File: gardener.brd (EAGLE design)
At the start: 73.5 x 55 mm, 37 parts, among them IC2 REG1117

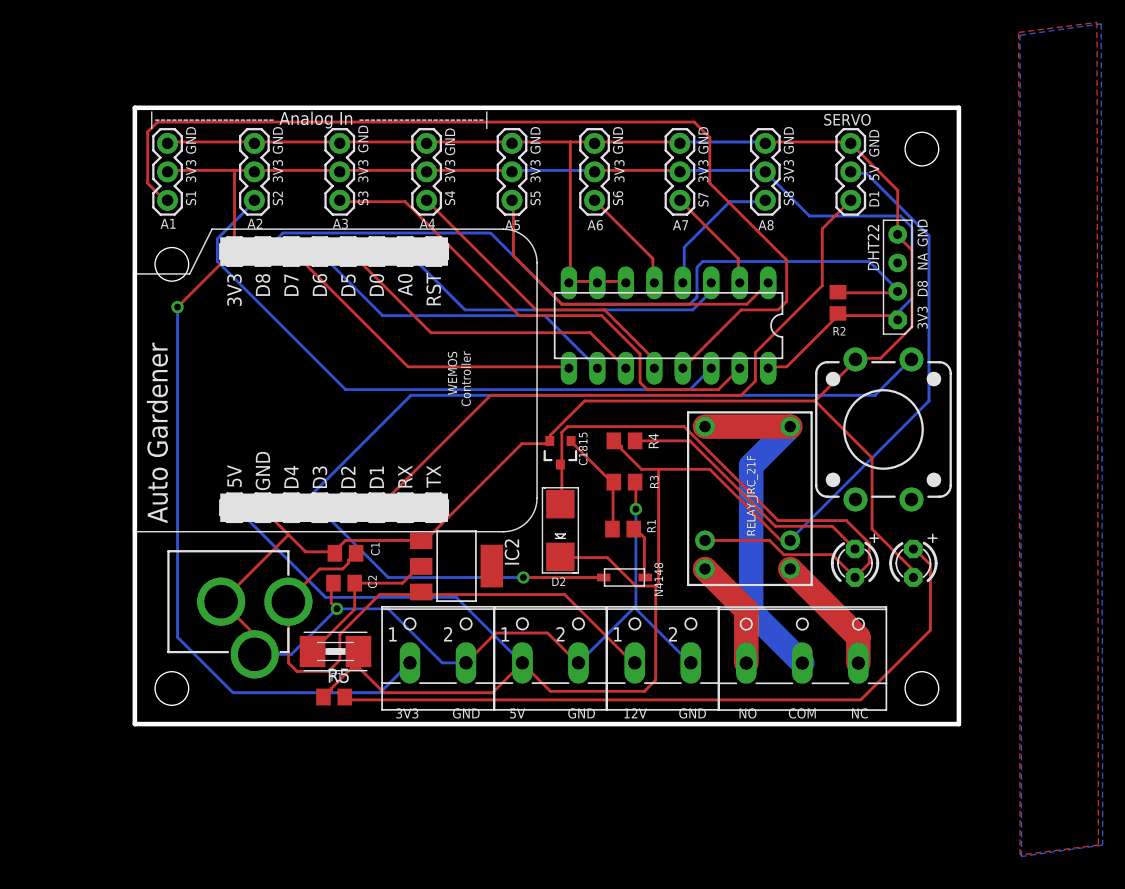
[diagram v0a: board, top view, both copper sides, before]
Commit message: Update design to add one more AMS1117 for servo
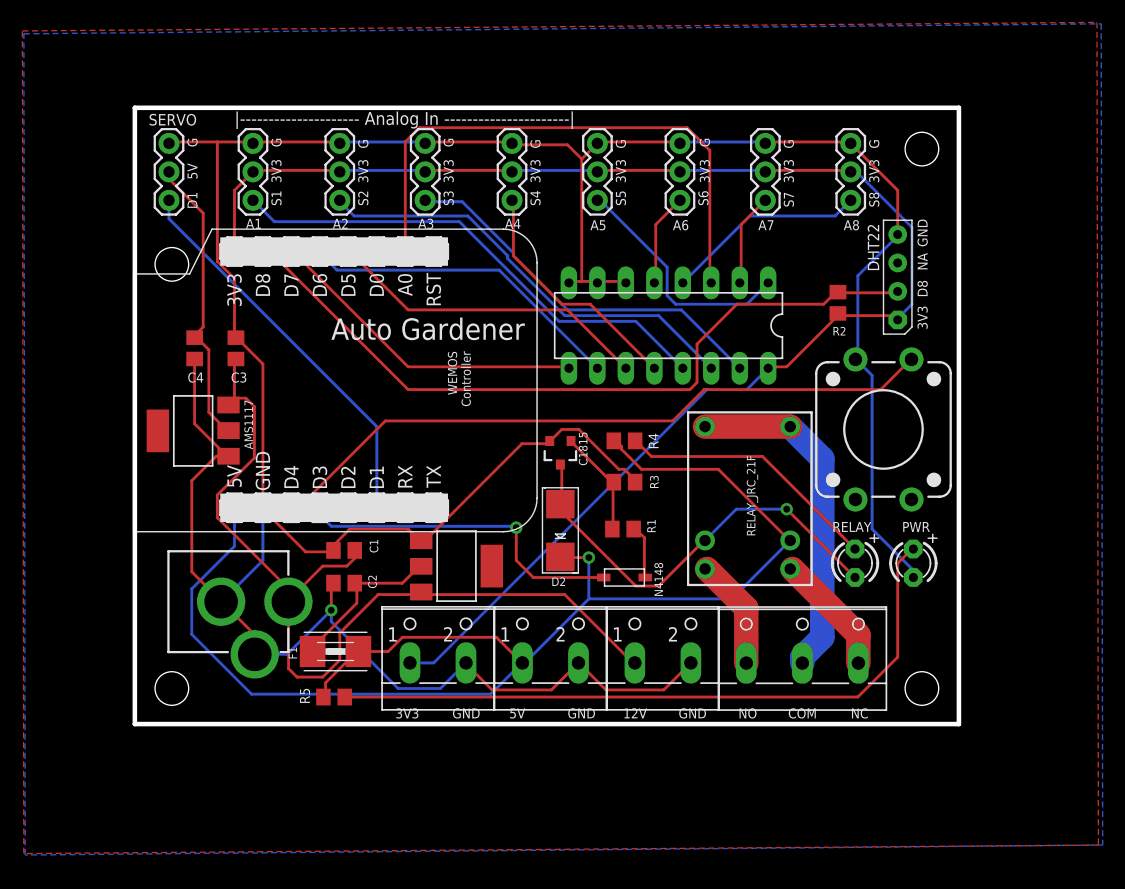
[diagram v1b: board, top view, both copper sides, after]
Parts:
- added C3: 100uF, rcl:C0805
- added C4: 22uF, rcl:C0805
- added IC1: AMS1117, burr-brown:SOT223
- IC2: value REG1117 -> AMS1117
- JP1: value POWER JACK 12V -> POWER IN 6-12V
- moved SERVO 60.8 mm to (3.30, 46.4)
- moved A5 7.62 mm to (41.5, 46.4)
- moved A6 7.62 mm to (48.9, 46.4)
- moved A8 7.62 mm to (64.1, 46.4)
- moved A2 7.62 mm to (18.5, 46.4)
- moved A1 7.62 mm to (10.8, 46.4)
- moved A3 7.62 mm to (26.2, 46.4)
- moved A4 7.62 mm to (33.9, 46.4)
- moved A7 7.62 mm to (56.5, 46.4)
- moved C1 0.28 mm to (18.9, 15.1)
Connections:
- new net 5V_MOTOR: C4.1, IC1.2, SERVO.2
- net 5V: no longer SERVO.2
- net GND: now also C3.2, C4.2, IC1.1
- net VIN: now also C3.1, IC1.3
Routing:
- net A1: track 87.3 -> 44.6 mm
- net 5V: track 157.2 -> 121.8 mm, vias 0 -> 1
- net GND: track 263.7 -> 296.0 mm, vias 2 -> 1
- net VIN: track 51.7 -> 82.4 mm
- net 5V_MOTOR: track 0.00 -> 26.2 mm
- net +3V3: track 159.6 -> 135.1 mm, vias 1 -> 0
- net D1: track 58.2 -> 35.2 mm
- net A0: track 31.0 -> 50.1 mm
- net N$1: track 56.9 -> 38.7 mm, vias 0 -> 1
- net A2: track 56.4 -> 39.6 mm
- net A3: track 45.0 -> 34.5 mm
- net A5: track 30.3 -> 21.5 mm
- net A8: track 12.2 -> 18.0 mm
- net A4: track 27.0 -> 21.7 mm
- net D8: track 69.9 -> 67.8 mm
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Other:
- board text added: "G"

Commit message: Update design to version 0.2
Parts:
- removed C1, C3: 100uF, rcl:C0805
- removed C2, C4: 22uF, rcl:C0805
- removed DHT22: (no value), RHT03_DHT-22_AM2302:AM2302
- removed F1: 1A/15V, adafruit:1812
- removed IC1, IC2: AMS1117, burr-brown:SOT223
- removed JP1: POWER IN 6-12V, SparkFun-Connectors:POWER_JACK_PTH
- removed R2: 10K, rcl:R0805
- removed S2: SWITCH-MOMENTARY-212MM, SparkFun-Electromechanical:TACTILE-PTH-12MM
- removed U$4: RELAY_JRC_21F, My Eagle Lib:MINIATURE_RELAY_JRC_21F
- removed X4: (no value), con-wago-500:W237-102
- added C5, C6: 100uF/35V, SparkFun-Passives:PANASONIC_D
- added CAP_BTN: (no value), SparkFun-Connectors:1X03
- added D3: SS34, SparkFun-DiscreteSemi:SMA-DIODE
- added IC4: LM2596S, national-semiconductor:TO263-5
- added JP2: POWER IN, SparkFun-Connectors:POWER_JACK_PTH
- added L3: 100uH, SparkFun-Passives:INDUCTOR_SDR1307
- added OLED: (no value), SparkFun-Connectors:1X04
- added RELAY: ZNS5106, relay:ZN5
- added SW_BTN: SWITCH-MOMENTARY-212MM, SparkFun-Electromechanical:TACTILE-PTH-12MM
- added WAKE: (no value), SparkFun-Connectors:1X02
- moved R5 64.0 mm to (75.9, 29.3), turned to 270 degrees
- moved D2 33.4 mm to (70.9, 24.0), turned to 0 degrees
- moved R4 28.7 mm to (72.3, 29.3), turned to 270 degrees
- moved R3 25.6 mm to (68.2, 29.3), turned to 90 degrees
- moved R1 24.5 mm to (65.0, 29.3), turned to 270 degrees
- moved C1815 24.5 mm to (62.7, 23.9), turned to 270 degrees
- moved N4148 24.4 mm to (61.7, 29.5), turned to 270 degrees
- moved LED2 19.1 mm to (80.0, 30.1), turned to 90 degrees
- moved LED1 18.5 mm to (80.0, 24.1)
- moved X1 17.5 mm to (75.9, 13.2), turned to 90 degrees
- moved X3 12.8 mm to (50.2, 6.73)
- moved U$2 10.1 mm to (80.5, 51.9)
- moved U$6 9.78 mm to (80.3, 2.54)
- moved X2 7.25 mm to (40.1, 6.73)
- moved U$5 6.99 mm to (3.43, 33.7)
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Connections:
- removed net 5V_MOTOR: C4.1, IC1.2, SERVO.2
- removed net VOUT: C2.1, F1.1, IC2.2
- new net N$9: D3.C, IC4.2, L3.P$1
- new net RST: U$3.RST, WAKE.1
- net +3V3: now also CAP_BTN.3, OLED.1, SW_BTN.3; no longer DHT22.VDD, R2.1, X4.1
- net 5V: now also C6.+, IC4.4, L3.P$2, RELAY.A1, SERVO.2; no longer F1.2, U$4.COIL1
- net COM: now also RELAY.11; no longer U$4.COM1, U$4.COM2
- net D0: now also WAKE.2
- net D2: now also N4148.A
- net D3: now also OLED.3; no longer N4148.A
- net D4: now also OLED.4; no longer S2.1
- net D8: now also CAP_BTN.2, SW_BTN.1; no longer DHT22.DATA, R2.2
- net GND: now also C5.-, C6.-, CAP_BTN.1, D3.A, IC4.3, IC4.5, JP2.GND, JP2.GNDBREAK, OLED.2; no longer C1.2, C2.2, C3.2, C4.2, DHT22.GND, IC1.1, IC2.1, JP1.GND, JP1.GNDBREAK, S2.3, X4.2
- net N$1: now also RELAY.A2; no longer U$4.COIL2
- net NC: now also RELAY.12; no longer U$4.NC
- net NO: now also RELAY.14; no longer U$4.NO
- net VIN: now also C5.+, IC4.1, JP2.PWR; no longer C1.1, C3.1, IC1.3, IC2.3, JP1.PWR
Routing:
- net 5V: track 121.8 -> 184.1 mm, vias 1 -> 3
- net N$4: track 61.1 -> 4.25 mm
- net D2: track 0.00 -> 49.9 mm, vias 0 -> 1
- net RST: track 0.00 -> 41.5 mm
- net D0: track 0.00 -> 36.5 mm
- net D6: track 29.0 -> 56.8 mm
- net N$9: track 0.00 -> 26.9 mm
- net 5V_MOTOR: track 26.2 -> 0.00 mm
- net D4: track 60.7 -> 34.9 mm
- net D8: track 67.8 -> 89.7 mm
- net D7: track 29.1 -> 47.8 mm
- net VOUT: track 14.5 -> 0.00 mm
- net N$3: track 23.6 -> 9.47 mm
- net GND: track 296.0 -> 282.9 mm, vias 1 -> 2
- net D5: track 29.1 -> 42.1 mm
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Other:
- board size 73.5 x 55 mm -> 83.1 x 55.1 mm
- board text added: "6-24V"
- board text added: "Auto Gardener v0.2"
- board text added: "D0"
- board text added: "D3"
- board text added: "D4"
- board text added: "RST"
- board text added: "SW_BTN"
- board text added: "VIN"
- board text removed: "12V"
- board text removed: "Auto Gardener"
- board text removed: "NA"
